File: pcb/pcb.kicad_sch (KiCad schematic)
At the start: 49 parts, among them J1 Barrel_Jack_Switch, J2 Conn_02x05_Odd_Even, J3 Conn_02x05_Odd_Even, Q1 RQ5P010SN, Q2 IRLML6244, SW1 SW_SPST, SW2 SW_SPST, SW3 SW_SPST, U1 L7805, U2 MCP1406/07, U3 MAX6921AWI, U4 MCP7940N-xSN, U5 Pico, Y1 32.768KHZ

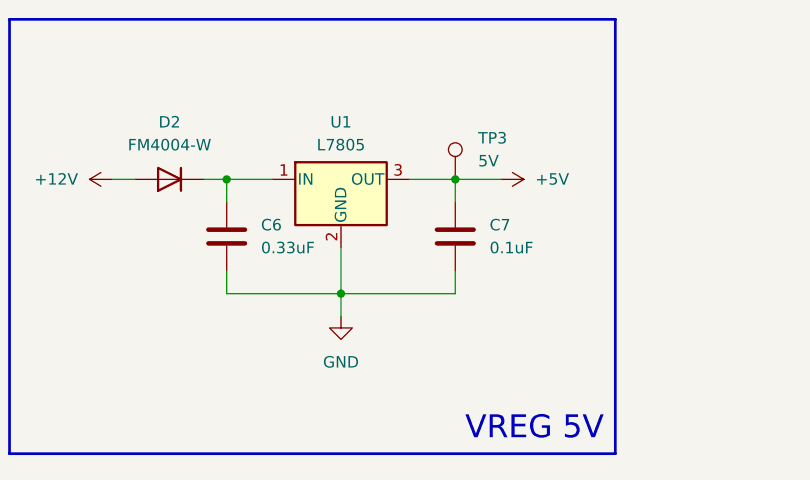
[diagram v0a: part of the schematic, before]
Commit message: exchanged lm7805 for vx7805
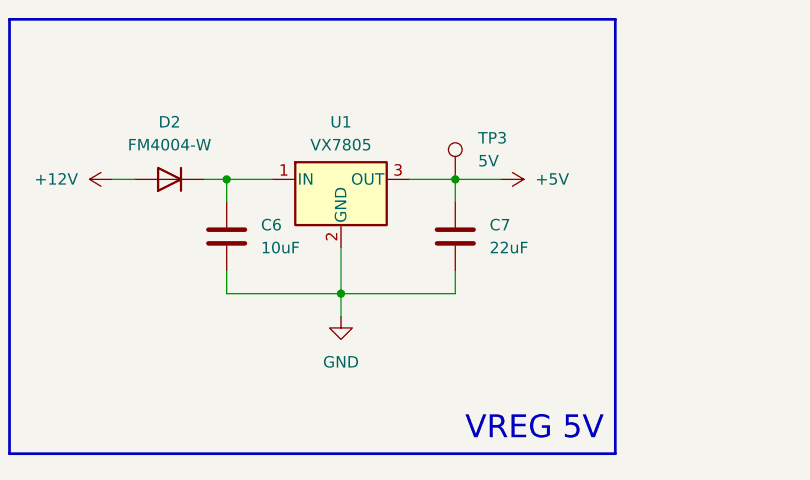
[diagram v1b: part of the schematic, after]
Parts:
- C6: value 0.33uF -> 10uF
- C7: value 0.1uF -> 22uF
- U1: value L7805 -> VX7805; footprint Package_TO_SOT_SMD:TO-263-2 -> vfd:VX7805
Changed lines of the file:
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@@
       (effects (font (size 1.27 1.27)) (justify left))
     )
-    (property "Value" "0.33uF" (at 217.17 44.45 0)
+    (property "Value" "10uF" (at 217.17 44.45 0)
       (effects (font (size 1.27 1.27)) (justify left))
     )
@@
       (effects (font (size 1.27 1.27)) (justify left))
     )
-    (property "Value" "0.1uF" (at 242.57 44.45 0)
+    (property "Value" "22uF" (at 242.57 44.45 0)
       (effects (font (size 1.27 1.27)) (justify left))
     )
@@
       (effects (font (size 1.27 1.27)))
     )
-    (property "Value" "L7805" (at 226.06 33.02 0)
-      (effects (font (size 1.27 1.27)))
-    )
-    (property "Footprint" "Package_TO_SOT_SMD:TO-263-2" (at 226.695 40.64 0)
+    (property "Value" "VX7805" (at 226.06 33.02 0)
+      (effects (font (size 1.27 1.27)))
+    )
+    (property "Footprint" "vfd:VX7805" (at 226.695 40.64 0)
       (effects (font (size 1.27 1.27) italic) (justify left) hide)
     )
